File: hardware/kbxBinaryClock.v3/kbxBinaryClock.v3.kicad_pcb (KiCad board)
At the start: 2 copper layers, 127 x 114.3 mm, 134 parts, among them J1 GS3, J2 Jack-DC, J3 Conn_01x06, J4 Conn_02x03_Odd_Even, P1 STM32_SWD_USART, Q1 2N7002, Q10 Q_NPN_BCE, Q11 Q_NPN_BCE, Q2 2N7002, Q3 2N7002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

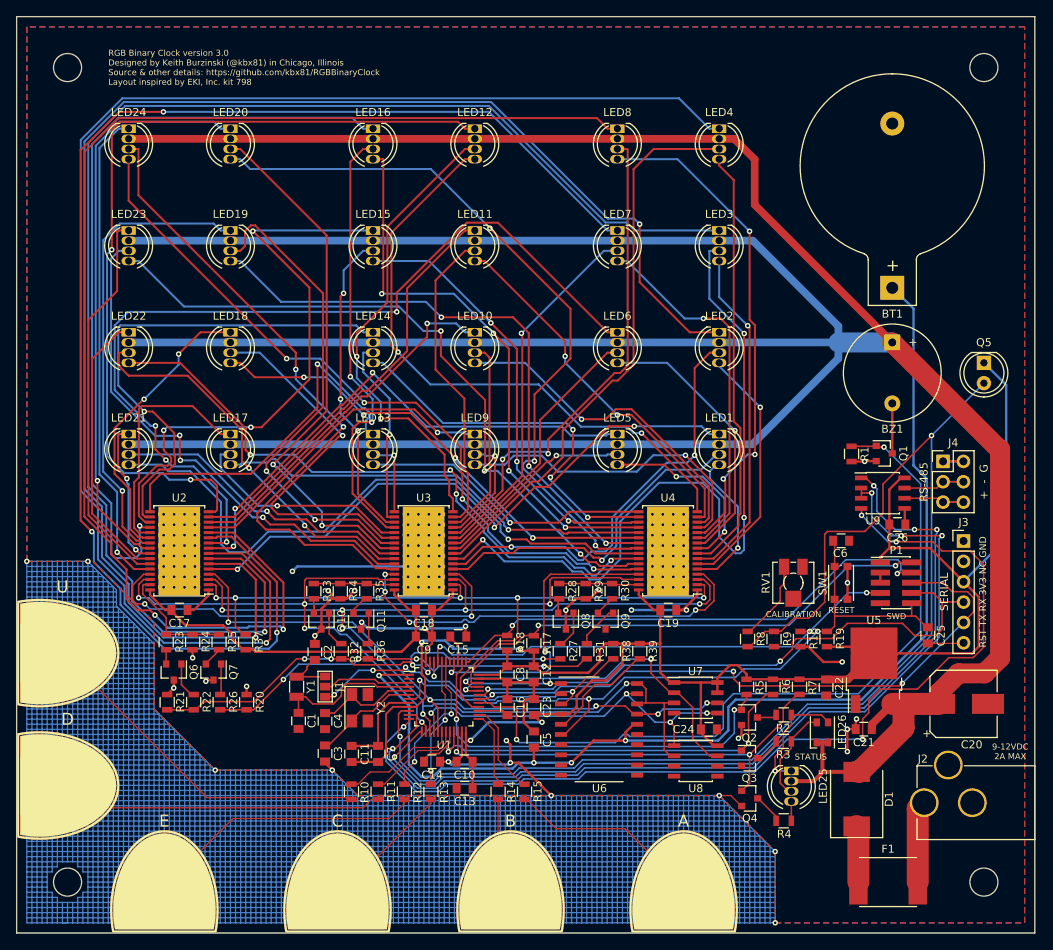
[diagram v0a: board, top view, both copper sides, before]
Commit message: Modified PCBs to accommodate a 16mm buzzer element
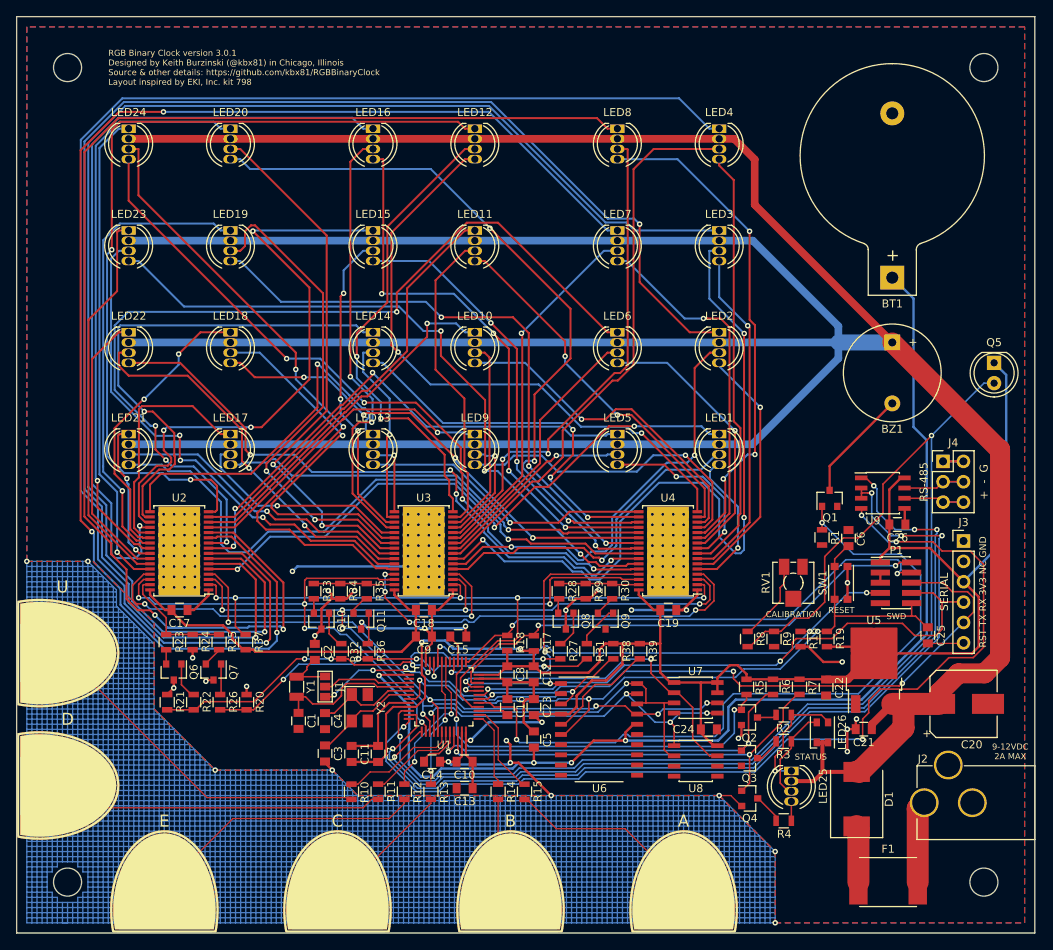
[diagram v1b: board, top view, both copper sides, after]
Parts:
- moved R1 11.0 mm to (194.4, 98.0)
- moved Q1 8.82 mm to (195.4, 93.1), turned to 90 degrees
- moved Q5 1.27 mm to (215.9, 76.2)
- moved BT1 1.27 mm to (203.2, 65.6)
- moved C6 0.98 mm to (197.7, 98.1), turned to 270 degrees
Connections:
- RV1 pad 3: (no net) -> GND
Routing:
- net Net-(BZ1-Pad2): track 5.61 -> 14.1 mm
- net BEEP: track 96.1 -> 92.1 mm
- net GND: track 6506.5 -> 6503.3 mm, vias 33 -> 32
- net +BATT: track 140.6 -> 141.9 mm
- net BOOT0: track 61.7 -> 62.5 mm
- net +3V3: track 289.9 -> 289.4 mm
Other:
- board text added: "RGB Binary Clock version 3.0.1 Designed by Keith Burzinski (@kbx81) in Chicago, Illinois Source & other details: https://github.com/kbx81/RGBBinaryClock Layout inspired by EKI, Inc. kit 798"
- board text removed: "RGB Binary Clock version 3.0 Designed by Keith Burzinski (@kbx81) in Chicago, Illinois Source & other details: https://github.com/kbx81/RGBBinaryClock Layout inspired by EKI, Inc. kit 798"

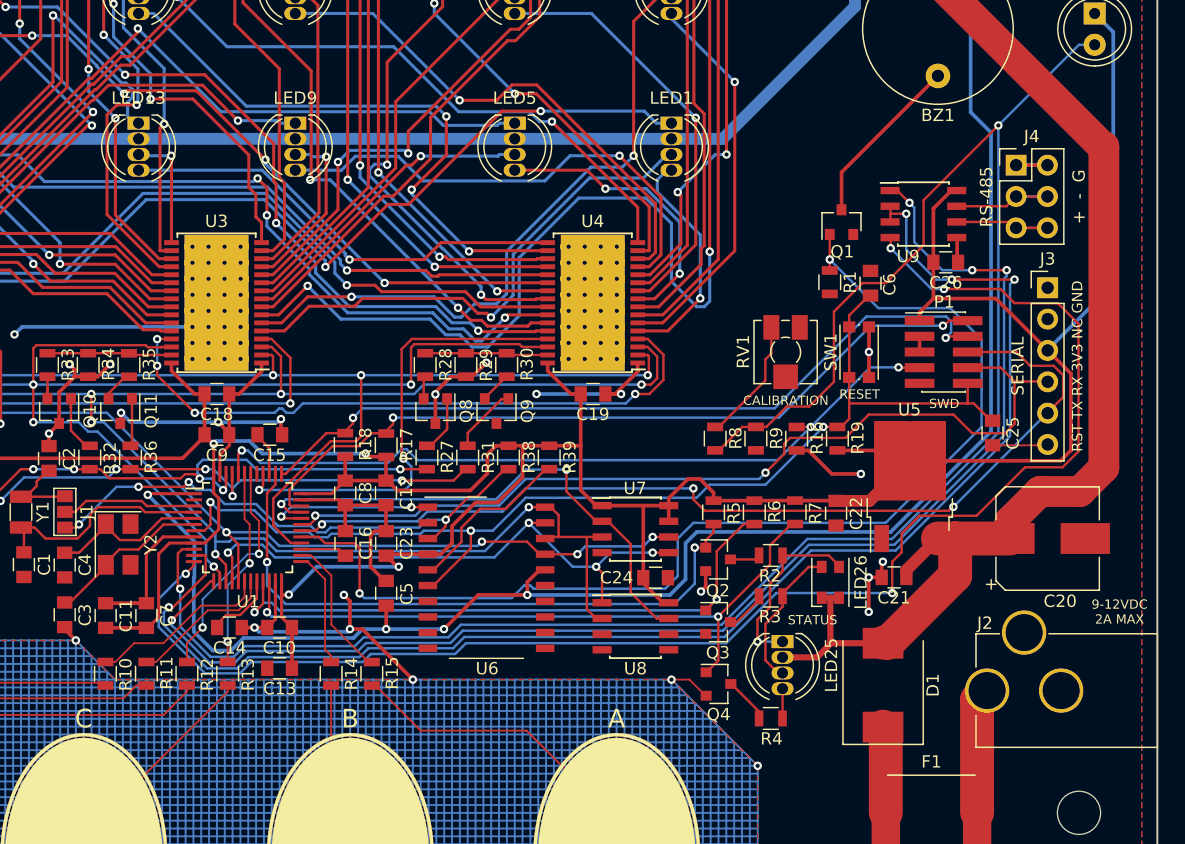
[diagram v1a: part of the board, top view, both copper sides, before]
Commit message: Added BoM, hw README, PCB tweaks
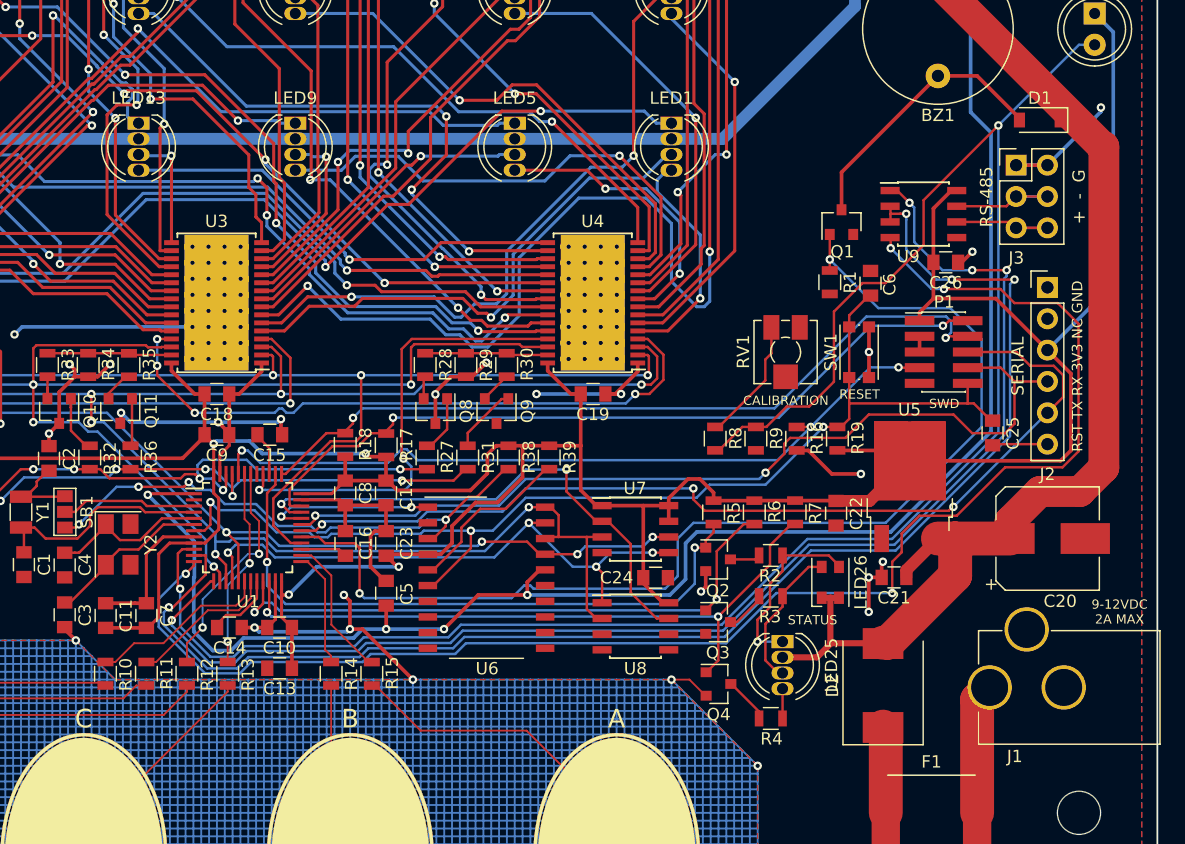
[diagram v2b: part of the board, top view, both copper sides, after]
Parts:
- removed J4: Conn_02x03_Odd_Even, Pin_Headers:Pin_Header_Straight_2x03_Pitch2.54mm
- added D2: S3A, Diodes_SMD:D_SMC, F.Cu at (198.8, 130.7)
- added SB1: GS3, Connectors:GS3, F.Cu at (132.5, 116.6)
- D1: value S3A -> 1N4148; footprint Diodes_SMD:D_SMC -> Diodes_SMD:D_SOD-123
- J1: value GS3 -> Jack-DC; footprint Connectors:GS3 -> kbxCustoms:BARREL_JACK
- J2: value Jack-DC -> Conn_01x06; footprint kbxCustoms:BARREL_JACK -> Pin_Headers:Pin_Header_Straight_1x06_Pitch2.54mm
- J3: value Conn_01x06 -> Conn_02x03_Odd_Even; footprint Pin_Headers:Pin_Header_Straight_1x06_Pitch2.54mm -> Pin_Headers:Pin_Header_Straight_2x03_Pitch2.54mm
- moved J1 76.3 mm to (207.4, 130.8), turned to 180 degrees
- moved D1 47.5 mm to (211.5, 84.8), turned to 180 degrees
- moved J2 33.0 mm to (212.1, 98.4), turned to 0 degrees
- moved J3 10.3 mm to (209.5, 88.5)
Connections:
- D1 pad 1: Net-(D1-Pad1) -> +V_IN
- D1 pad 2: +V_IN -> Net-(BZ1-Pad2)
- F1 pad 1: Net-(D1-Pad1) -> Net-(D2-Pad1)
- J1 pad 1: Net-(C2-Pad2) -> Net-(F1-Pad2)
- J1 pad 2: Net-(J1-Pad2) -> GND
- J1 pad 3: /MCU/OSC32_IN -> GND
- J2 pad 1: Net-(F1-Pad2) -> GND
- J2 pad 2: GND -> (no net)
- J2 pad 3: GND -> +3V3
- J3 pad 2: (no net) -> GND
- J3 pad 3: +3V3 -> Net-(J3-Pad3)
- J3 pad 4: /MCU/USART1_RX -> Net-(J3-Pad3)
- J3 pad 5: /MCU/USART1_TX -> Net-(J3-Pad5)
- J3 pad 6: Net-(C25-Pad1) -> Net-(J3-Pad5)
- U1 pad 3: Net-(J1-Pad2) -> Net-(SB1-Pad2)
- U9 pad 6: Net-(J4-Pad5) -> Net-(J3-Pad5)
- U9 pad 7: Net-(J4-Pad3) -> Net-(J3-Pad3)
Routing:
- net Net-(J1-Pad2): track 11.0 -> 0.00 mm
- net Net-(SB1-Pad2): track 0.00 -> 11.0 mm
- net Net-(J4-Pad3): track 10.2 -> 0.00 mm
- net Net-(J3-Pad3): track 0.00 -> 10.2 mm
- net Net-(J4-Pad5): track 10.1 -> 0.00 mm
- net Net-(J3-Pad5): track 0.00 -> 10.1 mm
- net Net-(BZ1-Pad2): track 14.1 -> 22.3 mm
- net Net-(D1-Pad1): track 7.21 -> 0.00 mm
- net Net-(D2-Pad1): track 0.00 -> 7.08 mm
- net GND: track 6503.3 -> 6509.3 mm, vias 32 -> 34
- net +V_IN: track 485.0 -> 489.5 mm

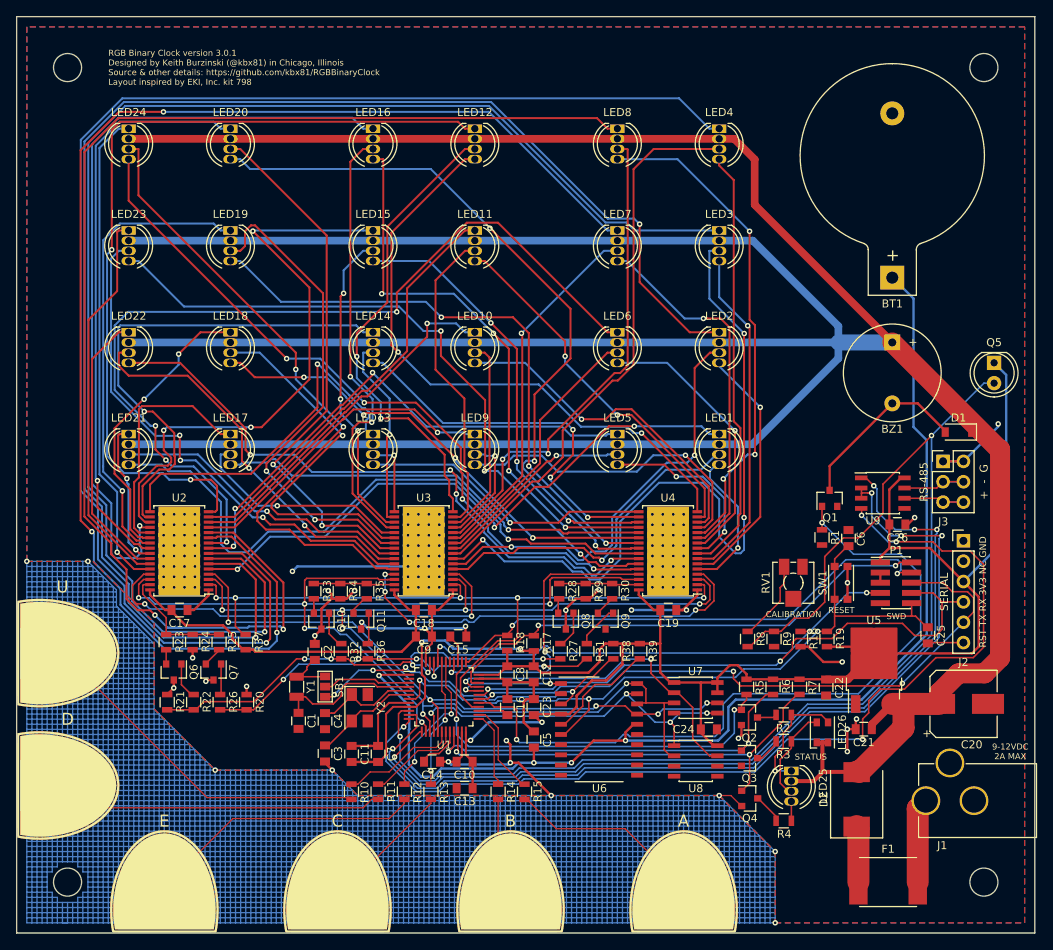
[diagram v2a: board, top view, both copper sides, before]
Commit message: Added disconnect on DS323x reset line
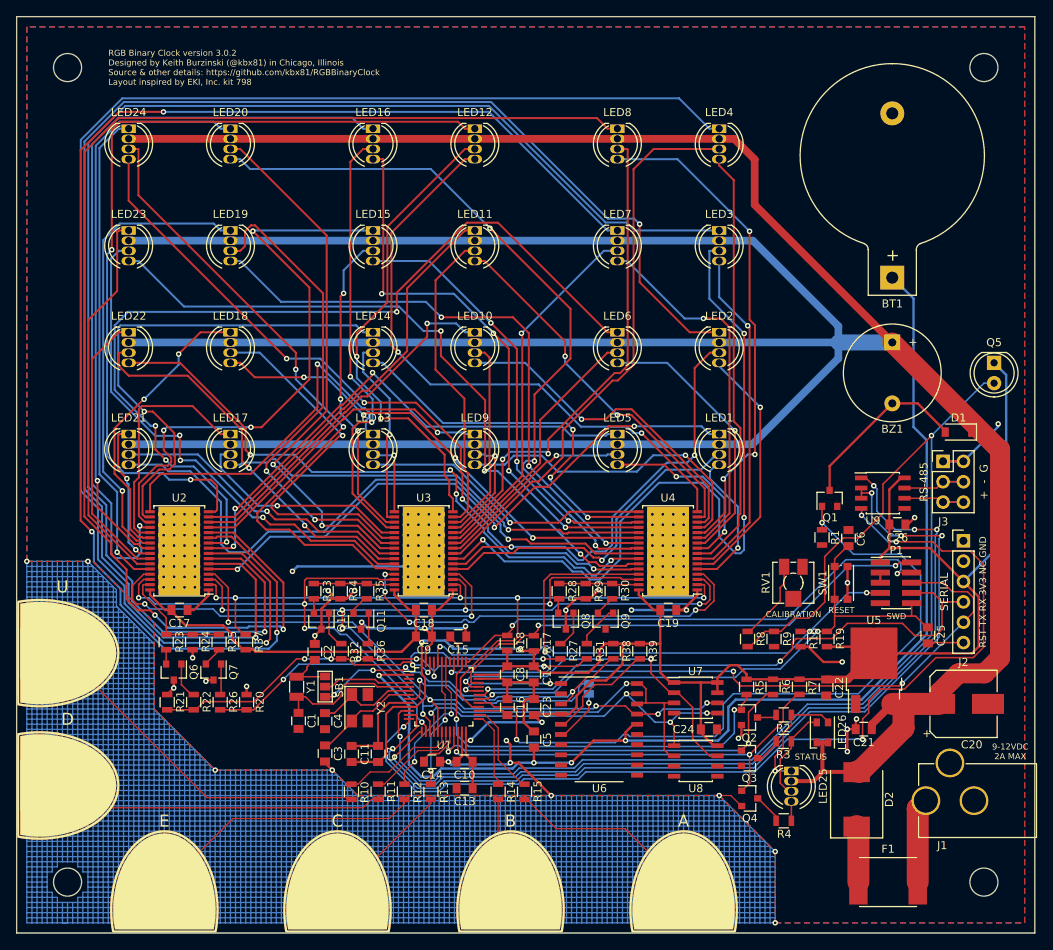
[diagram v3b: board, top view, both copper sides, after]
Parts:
- added SB2: GS2, Connectors:GS2, B.Cu at (165.4, 116.8)
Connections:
- J2 pad 2: (no net) -> Net-(J2-Pad2)
- P1 pad 9: (no net) -> Net-(P1-Pad9)
- U1 pad 2: (no net) -> Net-(U1-Pad2)
- U1 pad 41: (no net) -> Net-(U1-Pad41)
- U6 pad 6: /MCU/RESET -> Net-(SB2-Pad2)
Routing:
- net Net-(SB2-Pad2): track 0.00 -> 6.78 mm, vias 0 -> 1
- net /MCU/RESET: track 91.0 -> 85.4 mm, vias 3 -> 2
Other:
- board text added: "RGB Binary Clock version 3.0.2 Designed by Keith Burzinski (@kbx81) in Chicago, Illinois Source & other details: https://github.com/kbx81/RGBBinaryClock Layout inspired by EKI, Inc. kit 798"
- board text removed: "RGB Binary Clock version 3.0.1 Designed by Keith Burzinski (@kbx81) in Chicago, Illinois Source & other details: https://github.com/kbx81/RGBBinaryClock Layout inspired by EKI, Inc. kit 798"
